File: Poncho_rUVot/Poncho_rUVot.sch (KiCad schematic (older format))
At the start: 20 parts, among them J1 Screw_Terminal_01x03, K1 G5V-1, P10 Conn_01x04, P11 Conn_01x08, P3 Conn_01x03, P4 Conn_01x03, P5 Conn_01x04, P6 Conn_01x02, P7 Conn_01x02, P8 Conn_01x03, P9 Conn_01x06, Q1 BC548, Q2 BC548

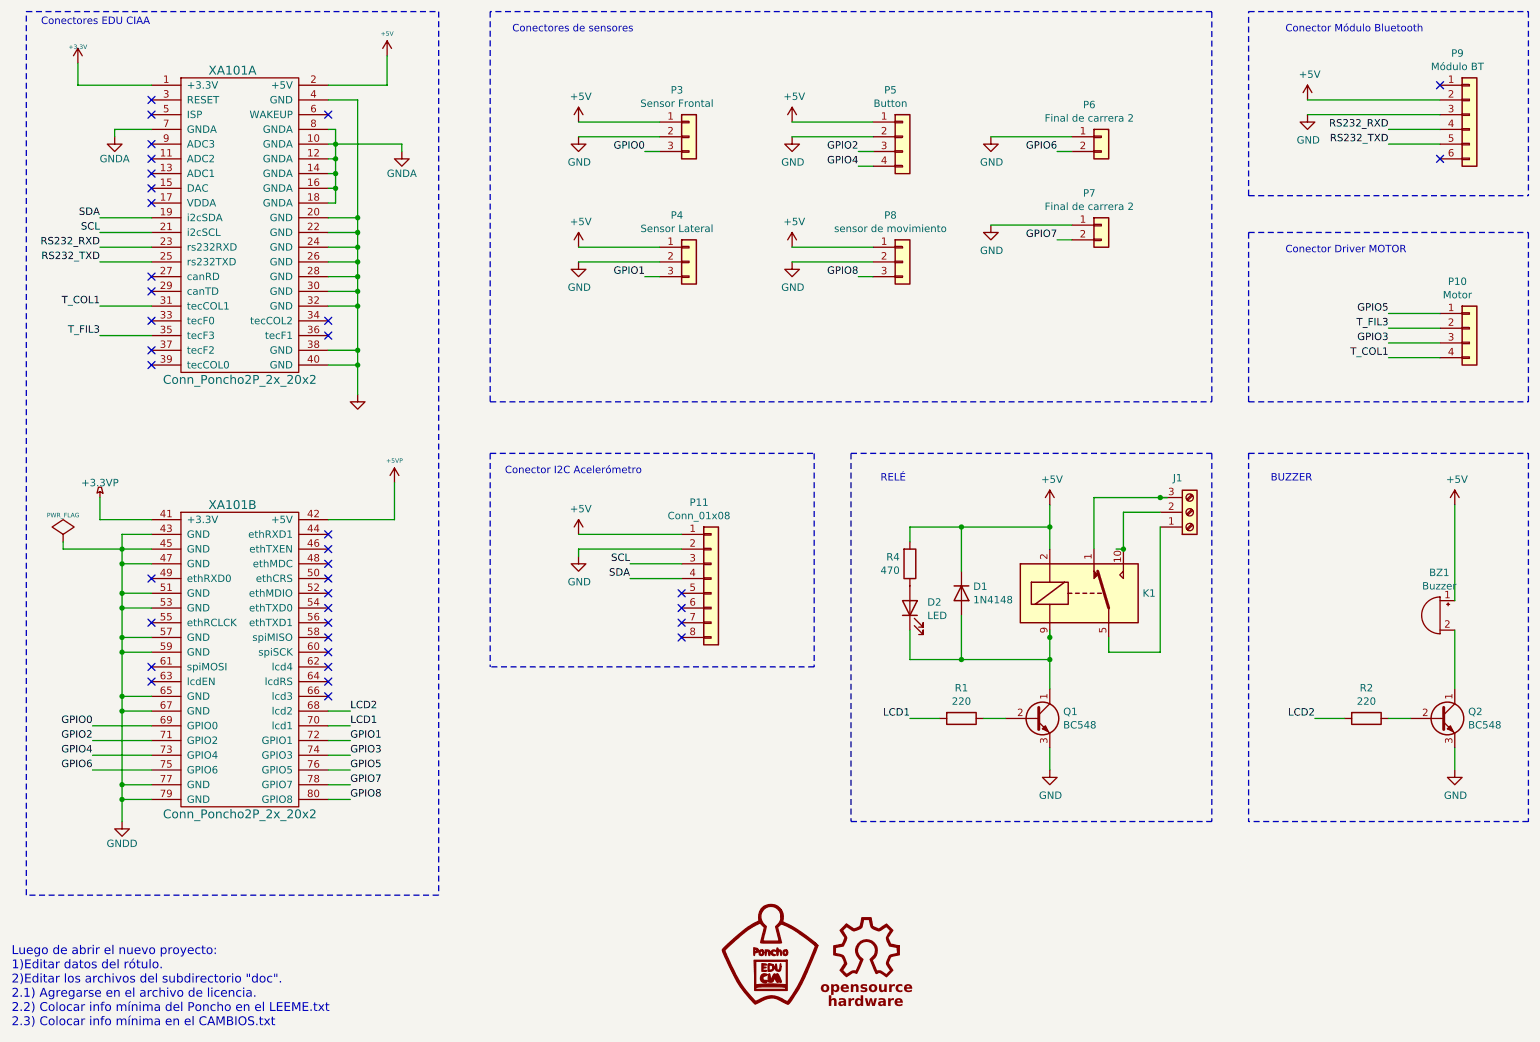
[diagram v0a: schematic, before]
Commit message: actualizo esquematico
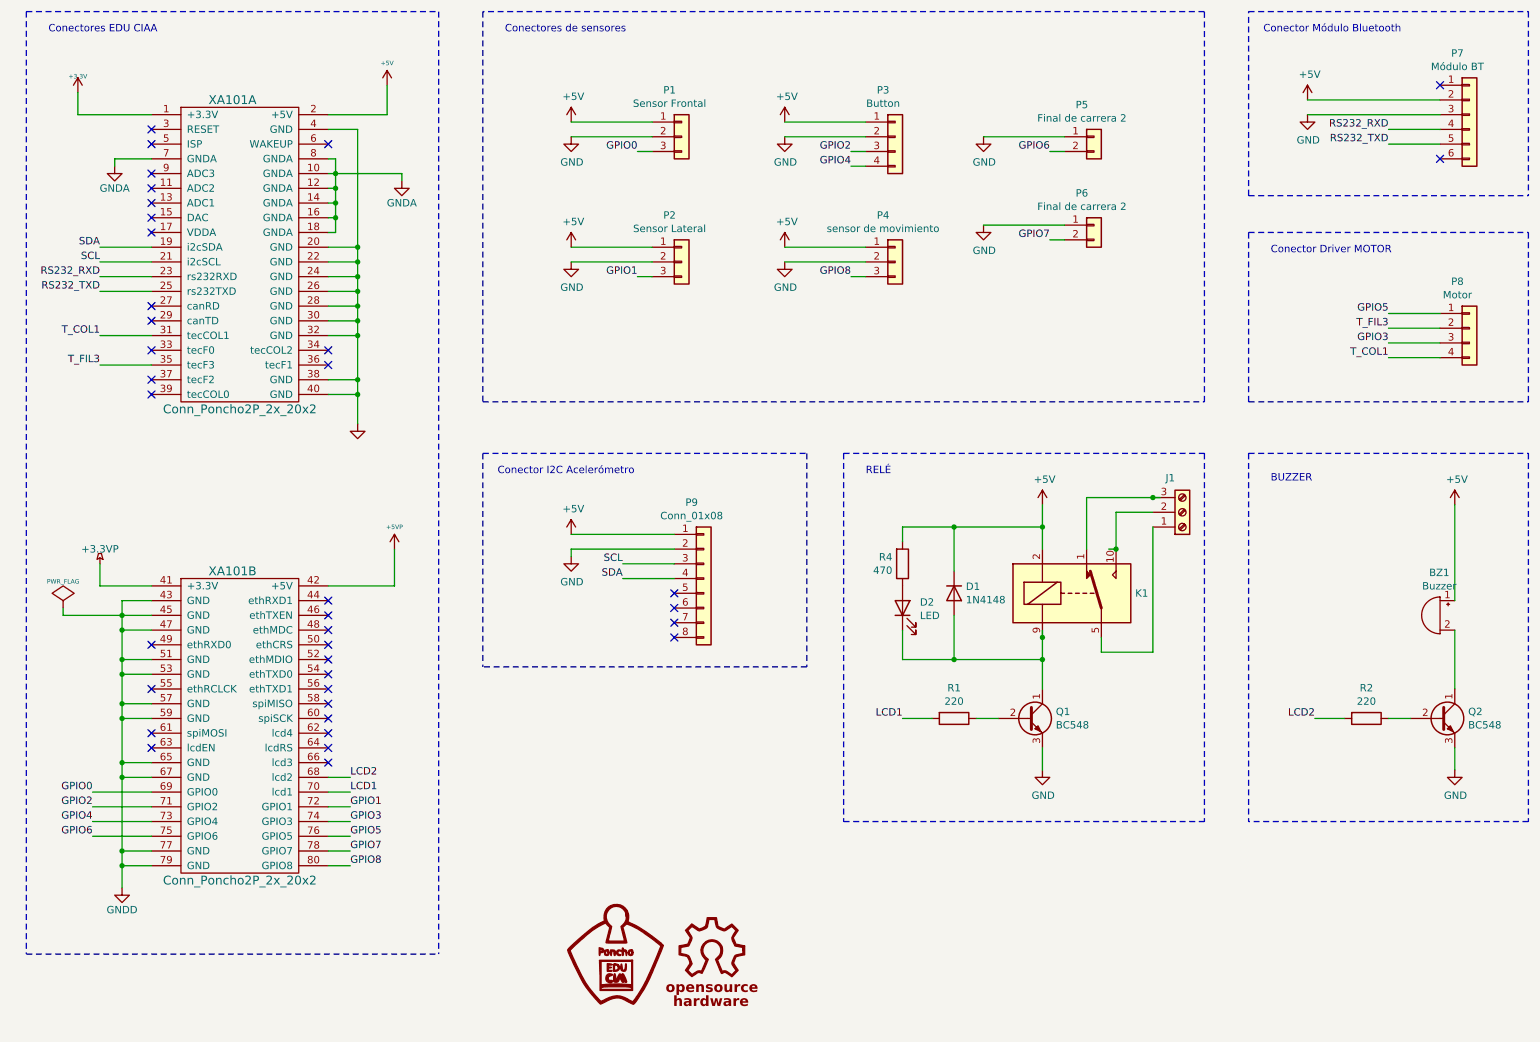
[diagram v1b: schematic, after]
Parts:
- renumbered P3 to P1, P4 to P2, P5 to P3, P8 to P4, P6 to P5, P7 to P6, P9 to P7, P10 to P8, P11 to P9
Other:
- note removed: "Luego de abrir el nuevo proyecto:\n1)Editar datos del rótulo.\n2)Editar los archivos del subdirectorio "doc".\n2.1) Agregarse en el archivo de licencia.\n2.2) Colocar info mínima del Poncho en el LEEME.txt\n2.3) Colocar info mínima en el CAMBIOS.txt"
- moved on the sheet: D1, D2, J1, K1, P1, P2, P3, P4, P5, P6, P9, Q1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
